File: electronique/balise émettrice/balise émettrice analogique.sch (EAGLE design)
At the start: 56 parts, among them IC1 TL084P, IC2 TL084P, J1 J7MM

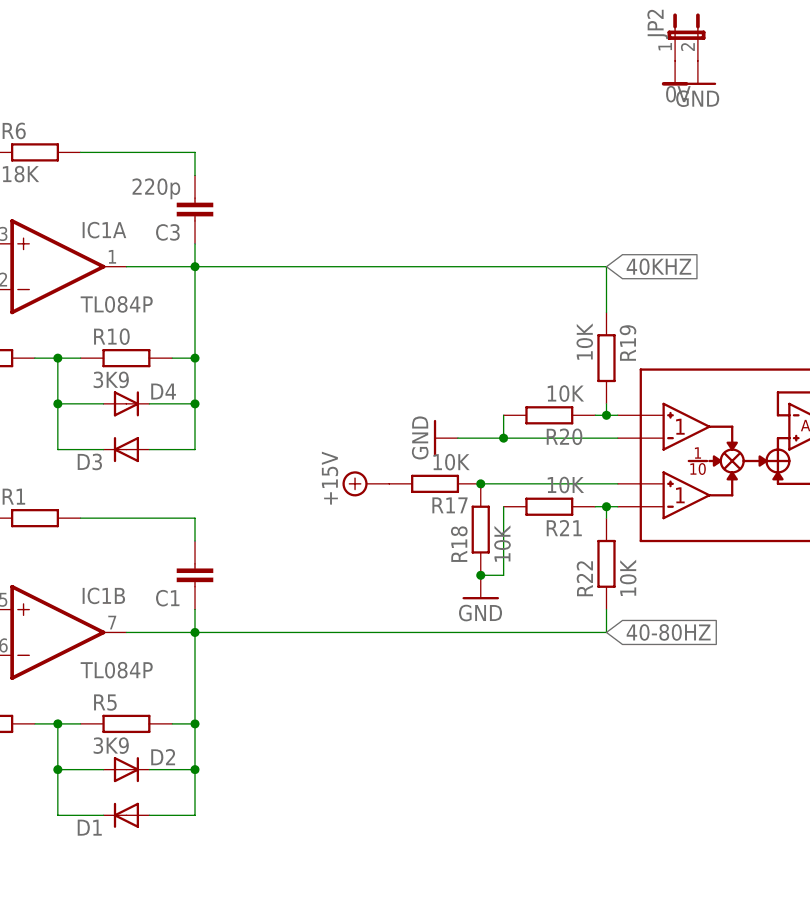
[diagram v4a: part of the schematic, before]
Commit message: maj mineure elec + ajout doc de l'elec
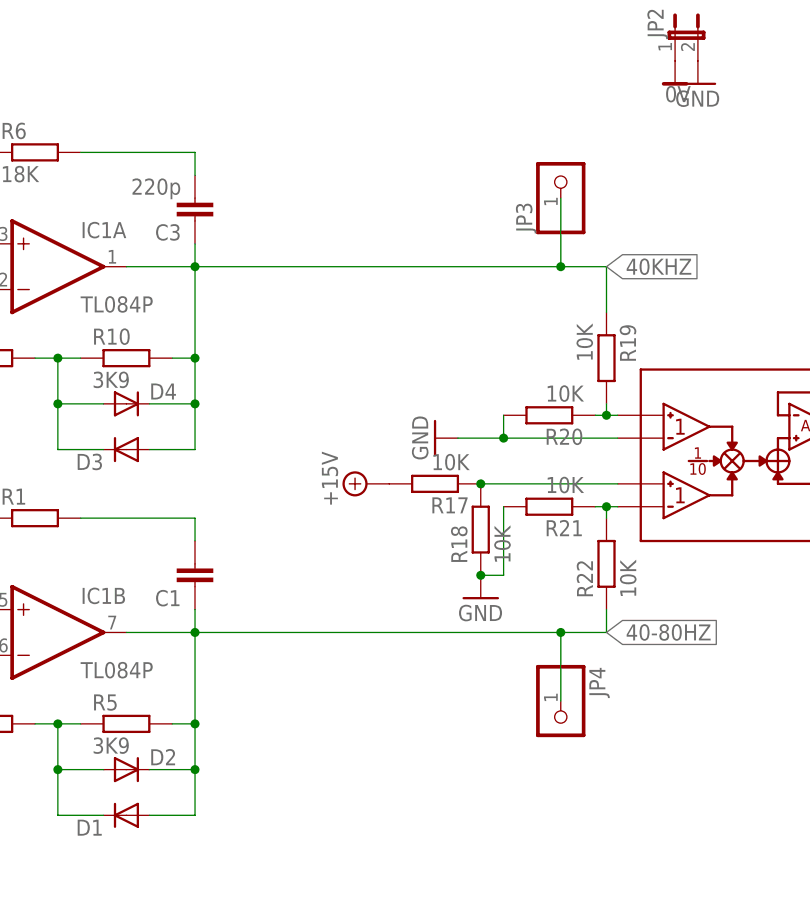
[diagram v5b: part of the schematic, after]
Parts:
- added JP3, JP4: (no value), pinhead:PINHD-1X1
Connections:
- net 40-80HZ: now also JP4.1
- net 40KHZ: now also JP3.1
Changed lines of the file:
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@@
 <grid distance="0.1" unitdist="inch" unit="inch" style="lines" multiple="1" display="no" altdistance="0.01" altunitdist="inch" altunit="inch"/>
 <layers>
-<layer number="1" name="Top" color="4" fill="1" visible="yes" active="no"/>
-<layer number="2" name="Route2" color="1" fill="3" visible="yes" active="no"/>
-<layer number="3" name="Route3" color="4" fill="3" visible="yes" active="no"/>
-<layer number="4" name="Route4" color="1" fill="4" visible="yes" active="no"/>
-<layer number="5" name="Route5" color="4" fill="4" visible="yes" active="no"/>
-<layer number="6" name="Route6" color="1" fill="8" visible="yes" active="no"/>
-<layer number="7" name="Route7" color="4" fill="8" visible="yes" active="no"/>
-<layer number="8" name="Route8" color="1" fill="2" visible="yes" active="no"/>
-<layer number="9" name="Route9" color="4" fill="2" visible="yes" active="no"/>
-<layer number="10" name="Route10" color="1" fill="7" visible="yes" active="no"/>
-<layer number="11" name="Route11" color="4" fill="7" visible="yes" active="no"/>
-<layer number="12" name="Route12" color="1" fill="5" visible="yes" active="no"/>
-<layer number="13" name="Route13" color="4" fill="5" visible="yes" active="no"/>
-<layer number="14" name="Route14" color="1" fill="6" visible="yes" active="no"/>
-<layer number="15" name="Route15" color="4" fill="6" visible="yes" active="no"/>
-<layer number="16" name="Bottom" color="1" fill="1" visible="yes" active="no"/>
-<layer number="17" name="Pads" color="2" fill="1" visible="yes" active="no"/>
-<layer number="18" name="Vias" color="2" fill="1" visible="yes" active="no"/>
-<layer number="19" name="Unrouted" color="6" fill="1" visible="yes" active="no"/>
-<layer number="20" name="Dimension" color="15" fill="1" visible="yes" active="no"/>
-<layer number="21" name="tPlace" color="7" fill="1" visible="yes" active="no"/>
-<layer number="22" name="bPlace" color="7" fill="1" visible="yes" active="no"/>
-<layer number="23" name="tOrigins" color="15" fill="1" visible="yes" active="no"/>
-<layer number="24" name="bOrigins" color="15" fill="1" visible="yes" active="no"/>
-<layer number="25" name="tNames" color="7" fill="1" visible="yes" active="no"/>
-<layer number="26" name="bNames" color="7" fill="1" visible="yes" active="no"/>
-<layer number="27" name="tValues" color="7" fill="1" visible="yes" active="no"/>
-<layer number="28" name="bValues" color="7" fill="1" visible="yes" active="no"/>
+<layer number="1" name="Top" color="4" fill="1" visible="no" active="no"/>
+<layer number="2" name="Route2" color="1" fill="3" visible="no" active="no"/>
+<layer number="3" name="Route3" color="4" fill="3" visible="no" active="no"/>
+<layer number="4" name="Route4" color="1" fill="4" visible="no" active="no"/>
+<layer number="5" name="Route5" color="4" fill="4" visible="no" active="no"/>
+<layer number="6" name="Route6" color="1" fill="8" visible="no" active="no"/>
+<layer number="7" name="Route7" color="4" fill="8" visible="no" active="no"/>
+<layer number="8" name="Route8" color="1" fill="2" visible="no" active="no"/>
+<layer number="9" name="Route9" color="4" fill="2" visible="no" active="no"/>
+<layer number="10" name="Route10" color="1" fill="7" visible="no" active="no"/>
+<layer number="11" name="Route11" color="4" fill="7" visible="no" active="no"/>
+<layer number="12" name="Route12" color="1" fill="5" visible="no" active="no"/>
+<layer number="13" name="Route13" color="4" fill="5" visible="no" active="no"/>
+<layer number="14" name="Route14" color="1" fill="6" visible="no" active="no"/>
+<layer number="15" name="Route15" color="4" fill="6" visible="no" active="no"/>
+<layer number="16" name="Bottom" color="1" fill="1" visible="no" active="no"/>
+<layer number="17" name="Pads" color="2" fill="1" visible="no" active="no"/>
+<layer number="18" name="Vias" color="2" fill="1" visible="no" active="no"/>
+<layer number="19" name="Unrouted" color="6" fill="1" visible="no" active="no"/>
+<layer number="20" name="Dimension" color="15" fill="1" visible="no" active="no"/>
+<layer number="21" name="tPlace" color="7" fill="1" visible="no" active="no"/>
+<layer number="22" name="bPlace" color="7" fill="1" visible="no" active="no"/>
+<layer number="23" name="tOrigins" color="15" fill="1" visible="no" active="no"/>
+<layer number="24" name="bOrigins" color="15" fill="1" visible="no" active="no"/>
+<layer number="25" name="tNames" color="7" fill="1" visible="no" active="no"/>
+<layer number="26" name="bNames" color="7" fill="1" visible="no" active="no"/>
+<layer number="27" name="tValues" color="7" fill="1" visible="no" active="no"/>
+<layer number="28" name="bValues" color="7" fill="1" visible="no" active="no"/>
 <layer number="29" name="tStop" color="7" fill="3" visible="no" active="no"/>
 <layer number="30" name="bStop" color="7" fill="6" visible="no" active="no"/>
@@
 <layer number="35" name="tGlue" color="7" fill="4" visible="no" active="no"/>
 <layer number="36" name="bGlue" color="7" fill="5" visible="no" active="no"/>
-<layer number="37" name="tTest" color="7" fill="1" visible="yes" active="no"/>
-<layer number="38" name="bTest" color="7" fill="1" visible="yes" active="no"/>
+<layer number="37" name="tTest" color="7" fill="1" visible="no" active="no"/>
+<layer number="38" name="bTest" color="7" fill="1" visible="no" active="no"/>
 <layer number="39" name="tKeepout" color="4" fill="11" visible="no" active="no"/>
 <layer number="40" name="bKeepout" color="1" fill="11" visible="no" active="no"/>
@@
 <layer number="44" name="Drills" color="7" fill="1" visible="no" active="no"/>
 <layer number="45" name="Holes" color="7" fill="1" visible="no" active="no"/>
-<layer number="46" name="Milling" color="3" fill="1" visible="yes" active="no"/>
-<layer number="47" name="Measures" color="7" fill="1" visible="yes" active="no"/>
-<layer number="48" name="Document" color="7" fill="1" visible="yes" active="no"/>
-<layer number="49" name="Reference" color="7" fill="1" visible="yes" active="no"/>
-<layer number="51" name="tDocu" color="7" fill="1" visible="yes" active="no"/>
-<layer number="52" name="bDocu" color="7" fill="1" visible="yes" active="no"/>
+<layer number="46" name="Milling" color="3" fill="1" visible="no" active="no"/>
+<layer number="47" name="Measures" color="7" fill="1" visible="no" active="no"/>
+<layer number="48" name="Document" color="7" fill="1" visible="no" active="no"/>
+<layer number="49" name="Reference" color="7" fill="1" visible="no" active="no"/>
+<layer number="51" name="tDocu" color="7" fill="1" visible="no" active="no"/>
+<layer number="52" name="bDocu" color="7" fill="1" visible="no" active="no"/>
 <layer number="91" name="Nets" color="2" fill="1" visible="yes" active="yes"/>
 <layer number="92" name="Busses" color="1" fill="1" visible="yes" active="yes"/>
@@
 </part>
 <part name="U$2" library="switch" deviceset="1RT" device=""/>
+<part name="JP3" library="pinhead" deviceset="PINHD-1X1" device=""/>
+<part name="JP4" library="pinhead" deviceset="PINHD-1X1" device=""/>
 </parts>
 <sheets>
@@
 </instance>
 <instance part="U$2" gate="G$1" x="93.98" y="119.38" rot="R270"/>
+<instance part="JP3" gate="G$1" x="109.22" y="60.96" rot="R90"/>
+<instance part="JP4" gate="G$1" x="109.22" y="0" rot="R270"/>
 </instances>
 <busses>
@@
 <pinref part="IC1" gate="A" pin="OUT"/>
 <pinref part="R19" gate="G$1" pin="1"/>
-<wire x1="68.58" y1="50.8" x2="114.3" y2="50.8" width="0.1524" layer="91"/>
+<wire x1="68.58" y1="50.8" x2="109.22" y2="50.8" width="0.1524" layer="91"/>
+<wire x1="109.22" y1="50.8" x2="114.3" y2="50.8" width="0.1524" layer="91"/>
 <wire x1="114.3" y1="50.8" x2="114.3" y2="45.72" width="0.1524" layer="91"/>
 <label x="114.3" y="50.8" size="1.778" layer="95" xref="yes"/>
+<pinref part="JP3" gate="G$1" pin="1"/>
+<wire x1="109.22" y1="58.42" x2="109.22" y2="50.8" width="0.1524" layer="91"/>
+<junction x="109.22" y="50.8"/>
 </segment>
 </net>
@@
 <junction x="68.58" y="10.16"/>
 <pinref part="IC1" gate="B" pin="OUT"/>
-<wire x1="68.58" y1="10.16" x2="114.3" y2="10.16" width="0.1524" layer="91"/>
+<wire x1="68.58" y1="10.16" x2="109.22" y2="10.16" width="0.1524" layer="91"/>
 <pinref part="R22" gate="G$1" pin="1"/>
+<wire x1="109.22" y1="10.16" x2="114.3" y2="10.16" width="0.1524" layer="91"/>
 <wire x1="114.3" y1="10.16" x2="114.3" y2="12.7" width="0.1524" layer="91"/>
 <label x="114.3" y="10.16" size="1.778" layer="95" xref="yes"/>
+<pinref part="JP4" gate="G$1" pin="1"/>
+<wire x1="109.22" y1="2.54" x2="109.22" y2="10.16" width="0.1524" layer="91"/>
+<junction x="109.22" y="10.16"/>
 </segment>
 </net>

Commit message: maj liste des composants
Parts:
- JP3, JP4, U$2: OC_FARNELL (none) -> unknown
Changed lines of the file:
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@@
 <attribute name="OC_FARNELL" value="unknown"/>
 </part>
-<part name="U$2" library="switch" deviceset="1RT" device=""/>
-<part name="JP3" library="pinhead" deviceset="PINHD-1X1" device=""/>
-<part name="JP4" library="pinhead" deviceset="PINHD-1X1" device=""/>
+<part name="U$2" library="switch" deviceset="1RT" device="">
+<attribute name="MF" value=""/>
+<attribute name="MPN" value=""/>
+<attribute name="OC_FARNELL" value="unknown"/>
+</part>
+<part name="JP3" library="pinhead" deviceset="PINHD-1X1" device="">
+<attribute name="MF" value=""/>
+<attribute name="MPN" value=""/>
+<attribute name="OC_FARNELL" value="unknown"/>
+</part>
+<part name="JP4" library="pinhead" deviceset="PINHD-1X1" device="">
+<attribute name="MF" value=""/>
+<attribute name="MPN" value=""/>
+<attribute name="OC_FARNELL" value="unknown"/>
+</part>
 </parts>
 <sheets>
@@
 <attribute name="MPN" x="17.78" y="17.78" size="1.778" layer="96" display="off"/>
 </instance>
-<instance part="U$2" gate="G$1" x="93.98" y="119.38" rot="R270"/>
-<instance part="JP3" gate="G$1" x="109.22" y="60.96" rot="R90"/>
-<instance part="JP4" gate="G$1" x="109.22" y="0" rot="R270"/>
+<instance part="U$2" gate="G$1" x="93.98" y="119.38" rot="R270">
+<attribute name="OC_FARNELL" x="93.98" y="119.38" size="1.778" layer="96" display="off"/>
+<attribute name="MF" x="93.98" y="119.38" size="1.778" layer="96" display="off"/>
+<attribute name="MPN" x="93.98" y="119.38" size="1.778" layer="96" display="off"/>
+</instance>
+<instance part="JP3" gate="G$1" x="109.22" y="60.96" rot="R90">
+<attribute name="OC_FARNELL" x="109.22" y="60.96" size="1.778" layer="96" display="off"/>
+<attribute name="MF" x="109.22" y="60.96" size="1.778" layer="96" display="off"/>
+<attribute name="MPN" x="109.22" y="60.96" size="1.778" layer="96" display="off"/>
+</instance>
+<instance part="JP4" gate="G$1" x="109.22" y="0" rot="R270">
+<attribute name="OC_FARNELL" x="109.22" y="0" size="1.778" layer="96" display="off"/>
+<attribute name="MF" x="109.22" y="0" size="1.778" layer="96" display="off"/>
+<attribute name="MPN" x="109.22" y="0" size="1.778" layer="96" display="off"/>
+</instance>
 </instances>
 <busses>
